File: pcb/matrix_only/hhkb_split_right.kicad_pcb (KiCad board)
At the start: 2 copper layers, 171.7 x 97.4 mm, 83 parts, among them SW1 CPG151101S11-2, SW10 CPG151101S11-2, SW11 CPG151101S11-2, SW12 CPG151101S11-2, SW13 CPG151101S11-2, SW14 CPG151101S11-2, SW15 CPG151101S11-2, SW16 CPG151101S11-2, SW17 CPG151101S11-2, SW18 CPG151101S11-2, SW19 CPG151101S11-2, SW2 CPG151101S11-2, SW20 CPG151101S11-2, SW21 CPG151101S11-2, SW22 CPG151101S11-2, SW23 CPG151101S11-2, SW24 CPG151101S11-2, SW25 CPG151101S11-2, SW26 CPG151101S11-2, SW27 CPG151101S11-2, SW28 CPG151101S11-2, SW29 CPG151101S11-2, SW3 CPG151101S11-2, SW30 CPG151101S11-2, SW31 CPG151101S11-2, SW32 CPG151101S11-2, SW33 CPG151101S11-2, SW34 CPG151101S11-2, SW4 CPG151101S11-2, SW5 CPG151101S11-2, SW6 CPG151101S11-2, SW7 CPG151101S11-2, SW8 CPG151101S11-2, SW9 CPG151101S11-2, U1 74LVC595, U2 74LVC595

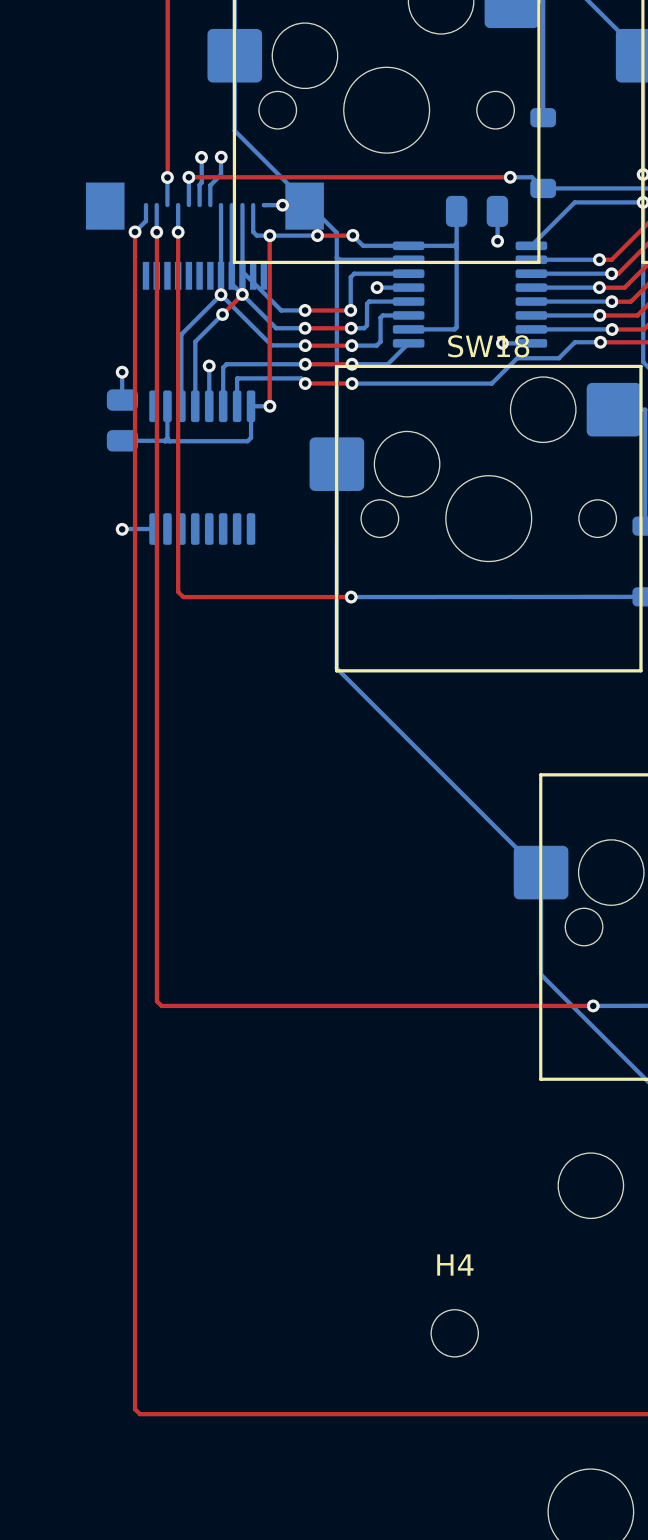
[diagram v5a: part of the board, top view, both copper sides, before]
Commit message: #19 右の J_DB 周りを利用者が引き直し、3 基板とも DRC 0 / 未配線 0
- COL0 の斜め線が回した J_DB の MP パッドを横切っていたのを MP の外（x=81 → y=82.3、SW10 の穴から 0.25mm 以上）へ逃がした
- φ0.5 の GND ビア 1 個を φ0.6 に
- 検査 457 緑・3 赤（右 J_DB とソケットの保守的占有範囲の重なり 1.63mm＝利用者の判断、露出ビアの打ち直し）。open-gaps #19 に記録
- 部品記録・DRC 記録・証拠ページを更新。gen_case.py の別セッションの変更は含めない

Co-Authored-By: Claude Fable 5 <noreply@anthropic.com>
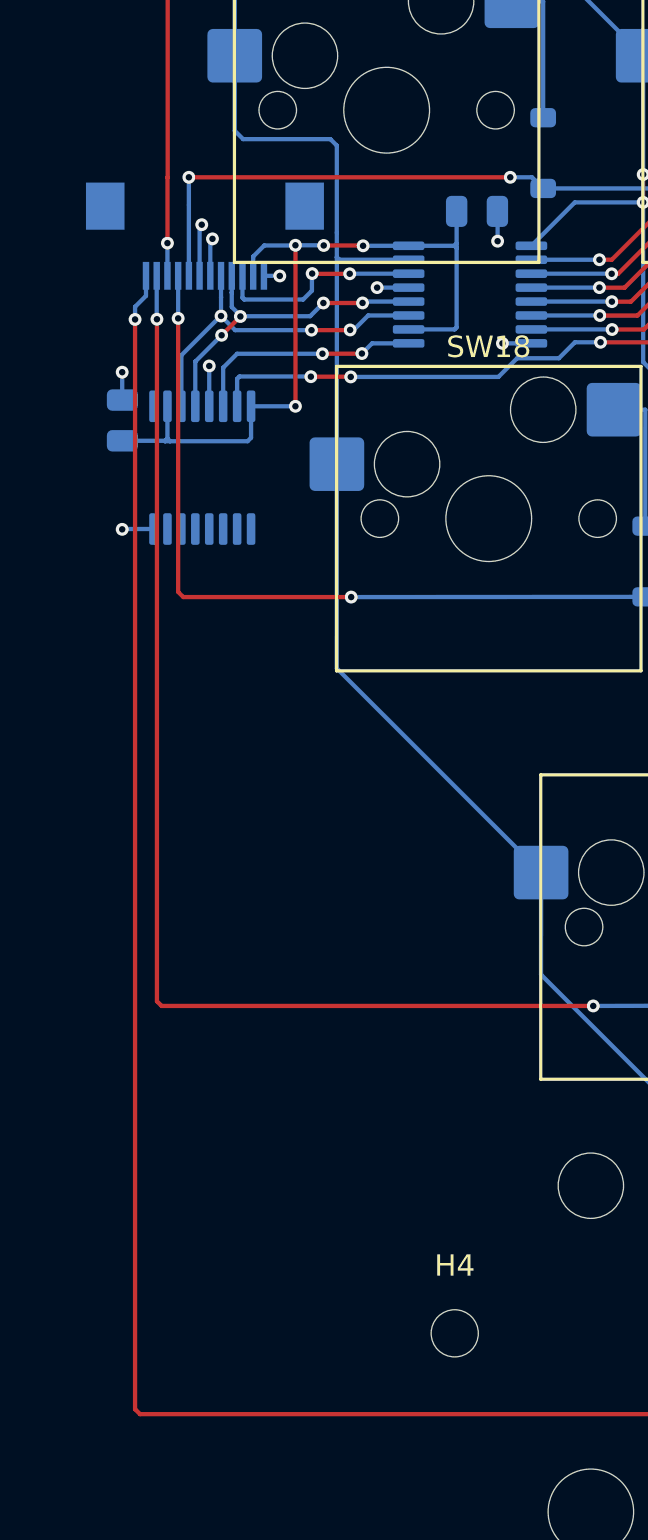
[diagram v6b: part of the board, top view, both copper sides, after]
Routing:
- net SPI_SCK: track 21.3 -> 16.2 mm
- net CS: track 20.0 -> 15.3 mm
- net SPI_MOSI: track 13.2 -> 9.78 mm
- net ROW_D: track 198.1 -> 194.8 mm
- net ROW_C: track 180.0 -> 183.3 mm
- net ROW_A: track 156.1 -> 159.4 mm
- net ROW_E: track 170.8 -> 167.5 mm
- net ROW_B: track 166.1 -> 162.8 mm
- net COL0: track 95.5 -> 97.9 mm
- net SPARE2: track 2.45 -> 1.77 mm

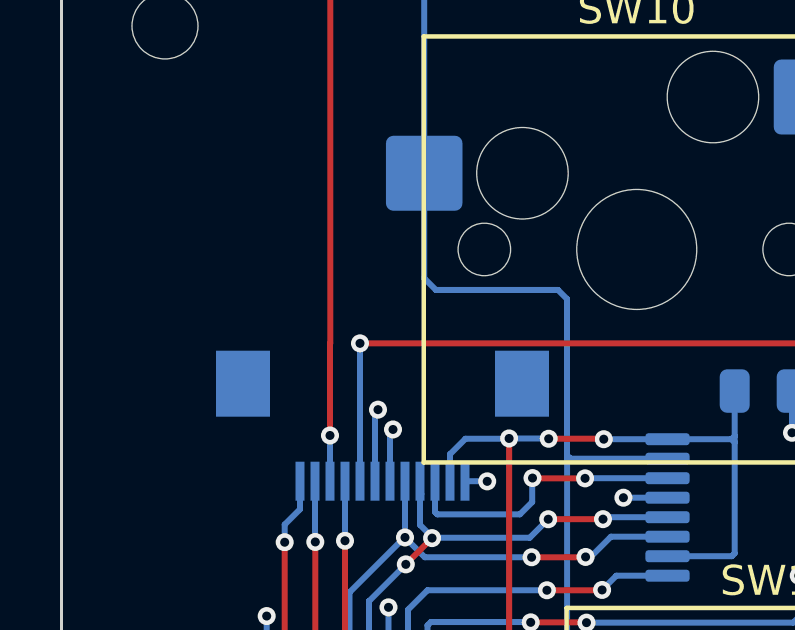
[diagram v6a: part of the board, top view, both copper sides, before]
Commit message: #49 利用者が左右の露出ビア（SPARE/SPARE2）を打ち直し。右の COL0 迂回と GND ビア径を当て直し、3 基板とも DRC 0
- 左右とも SPARE/SPARE2 が露出できるようになった（左 SCK は未だ）
- ⚠️ 打った場所はコネクタの奥側＝ケーブルの通り道。南側への移動を提案（open-gaps #19）

Co-Authored-By: Claude Fable 5 <noreply@anthropic.com>
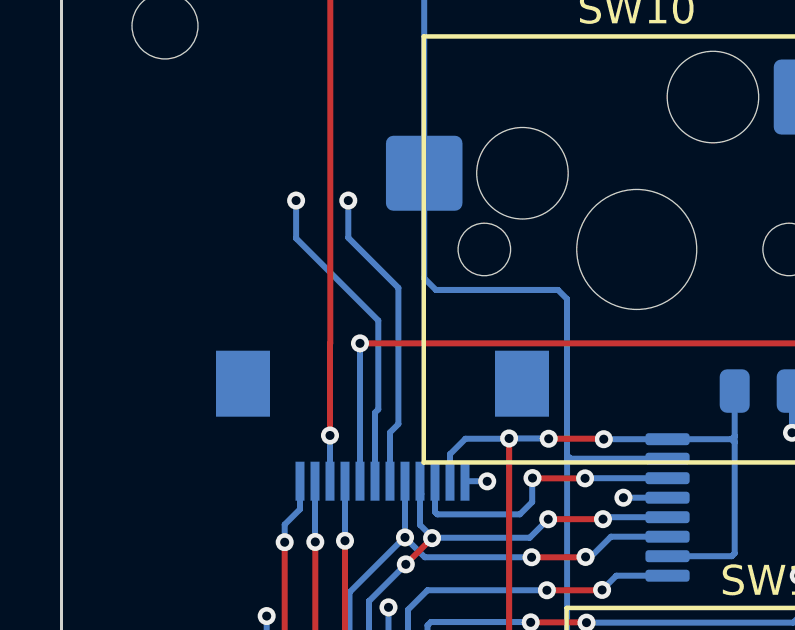
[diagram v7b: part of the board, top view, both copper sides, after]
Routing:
- net SPARE2: track 1.77 -> 10.2 mm
- net SPARE: track 2.43 -> 10.5 mm
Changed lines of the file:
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@@
+	)
+	(segment
+		(start 81 82.6)
+		(end 80.7 82.3)
+		(width 0.2)
+		(layer "B.Cu")
+		(net "COL0")
+	)
+	(segment
+		(start 81.0025 97.46)
+		(end 81.0025 88.0425)
+		(width 0.2)
+		(layer "B.Cu")
+		(net "COL0")
+	)
+	(segment
+		(start 81.0025 97.46)
+		(end 81 106.985)
+		(width 0.2)
+		(layer "B.Cu")
+		(net "COL0")
+	)
+	(segment
+		(start 81.12 87.925)
+		(end 81 87.81)
+		(width 0.2)
+		(layer "B.Cu")
+		(net "COL0")
+	)
+	(segment
+		(start 81 87.81)
+		(end 81 86.67)
+		(width 0.2)
+		(layer "B.Cu")
+		(net "COL0")
 	)
 	(segment
@@
 	)
 	(segment
-		(start 81.0025 97.46)
-		(end 81.0025 88.0425)
-		(width 0.2)
-		(layer "B.Cu")
-		(net "COL0")
-	)
-	(segment
-		(start 81.0025 97.46)
-		(end 81 106.985)
-		(width 0.2)
-		(layer "B.Cu")
-		(net "COL0")
-	)
-	(segment
-		(start 81.12 87.925)
-		(end 81 87.81)
+		(start 66.715 62.86)
+		(end 66.715 59.36)
 		(width 0.2)
 		(layer "B.Cu")
@@
 	)
 	(segment
+		(start 76.24 72.385)
+		(end 66.715 62.86)
+		(width 0.2)
+		(layer "B.Cu")
+		(net "COL0")
+	)
+	(segment
+		(start 84.35 87.925)
+		(end 81.12 87.925)
+		(width 0.2)
+		(layer "B.Cu")
+		(net "COL0")
+	)
+	(segment
+		(start 90.525 121.27)
+		(end 104.815 135.56)
+		(width 0.2)
+		(layer "B.Cu")
+		(net "COL0")
+	)
+	(segment
+		(start 81 88.04)
+		(end 81 87.81)
+		(width 0.2)
+		(layer "B.Cu")
+		(net "COL0")
+	)
+	(segment
+		(start 90.5275 116.51)
+		(end 90.525 121.27)
+		(width 0.2)
+		(layer "B.Cu")
+		(net "COL0")
+	)
+	(segment
+		(start 81 106.985)
+		(end 90.5275 116.51)
+		(width 0.2)
+		(layer "B.Cu")
+		(net "COL0")
+	)
+	(segment
+		(start 81.12 87.925)
+		(end 81 88.04)
+		(width 0.2)
+		(layer "B.Cu")
+		(net "COL0")
+	)
+	(segment
+		(start 76.24 81.91)
+		(end 76.24 72.385)
+		(width 0.2)
+		(layer "B.Cu")
+		(net "COL0")
+	)
+	(segment
 		(start 80.7 82.3)
 		(end 76.63 82.3)
@@
 	)
 	(segment
-		(start 66.715 62.86)
-		(end 66.715 59.36)
-		(width 0.2)
-		(layer "B.Cu")
-		(net "COL0")
-	)
-	(segment
-		(start 76.24 72.385)
-		(end 66.715 62.86)
-		(width 0.2)
-		(layer "B.Cu")
-		(net "COL0")
-	)
-	(segment
-		(start 84.35 87.925)
-		(end 81.12 87.925)
-		(width 0.2)
-		(layer "B.Cu")
-		(net "COL0")
-	)
-	(segment
-		(start 90.525 121.27)
-		(end 104.815 135.56)
-		(width 0.2)
-		(layer "B.Cu")
-		(net "COL0")
-	)
-	(segment
-		(start 81 82.6)
-		(end 80.7 82.3)
-		(width 0.2)
-		(layer "B.Cu")
-		(net "COL0")
-	)
-	(segment
-		(start 81 88.04)
-		(end 81 87.81)
-		(width 0.2)
-		(layer "B.Cu")
-		(net "COL0")
-	)
-	(segment
-		(start 81 87.81)
-		(end 81 86.67)
-		(width 0.2)
-		(layer "B.Cu")
-		(net "COL0")
-	)
-	(segment
-		(start 90.5275 116.51)
-		(end 90.525 121.27)
-		(width 0.2)
-		(layer "B.Cu")
-		(net "COL0")
-	)
-	(segment
-		(start 81 106.985)
-		(end 90.5275 116.51)
-		(width 0.2)
-		(layer "B.Cu")
-		(net "COL0")
-	)
-	(segment
-		(start 81.12 87.925)
-		(end 81 88.04)
-		(width 0.2)
-		(layer "B.Cu")
-		(net "COL0")
-	)
-	(segment
-		(start 76.24 81.91)
-		(end 76.24 72.385)
-		(width 0.2)
-		(layer "B.Cu")
-		(net "COL0")
-	)
-	(segment
 		(start 81.1 56.82)
 		(end 81.1 62.25)
@@
 	)
 	(via
-		(at 74.699999 86.29)
+		(at 71.97 79.32)
 		(size 0.6)
 		(drill 0.3)
@@
 	)
 	(segment
-		(start 74.699999 86.29)
-		(end 74.599999 86.39)
+		(start 71.97 80.58)
+		(end 74.71 83.32)
+		(width 0.2)
+		(layer "B.Cu")
+		(net "SPARE")
+	)
+	(segment
+		(start 71.97 79.32)
+		(end 71.97 80.58)
 		(width 0.2)
 		(layer "B.Cu")
@@
 		(net "SPARE")
 	)
-	(via
-		(at 75.199999 86.95)
-		(size 0.6)
-		(drill 0.3)
-		(layers "F.Cu" "B.Cu")
+	(segment
+		(start 74.71 86.279999)
+		(end 74.599999 86.39)
+		(width 0.2)
+		(layer "B.Cu")
+		(net "SPARE")
+	)
+	(segment
+		(start 74.71 83.32)
+		(end 74.71 86.279999)
+		(width 0.2)
+		(layer "B.Cu")
+		(net "SPARE")
+	)
+	(via
+		(at 73.71 79.32)
+		(size 0.6)
+		(drill 0.3)
+		(layers "F.Cu" "B.Cu")
+		(net "SPARE2")
+	)
+	(segment
+		(start 73.71 80.56)
+		(end 75.38 82.23)
+		(width 0.2)
+		(layer "B.Cu")
 		(net "SPARE2")
 	)
@@
 	)
 	(segment
-		(start 75.199999 86.95)
+		(start 75.38 82.23)
+		(end 75.38 86.769999)
+		(width 0.2)
+		(layer "B.Cu")
+		(net "SPARE2")
+	)
+	(segment
+		(start 75.38 86.769999)
 		(end 75.099999 87.05)
 		(width 0.2)
 		(layer "B.Cu")
+		(net "SPARE2")
+	)
+	(segment
+		(start 73.71 79.32)
+		(end 73.71 80.56)
+		(width 0.2)
+		(layer "B.Cu")

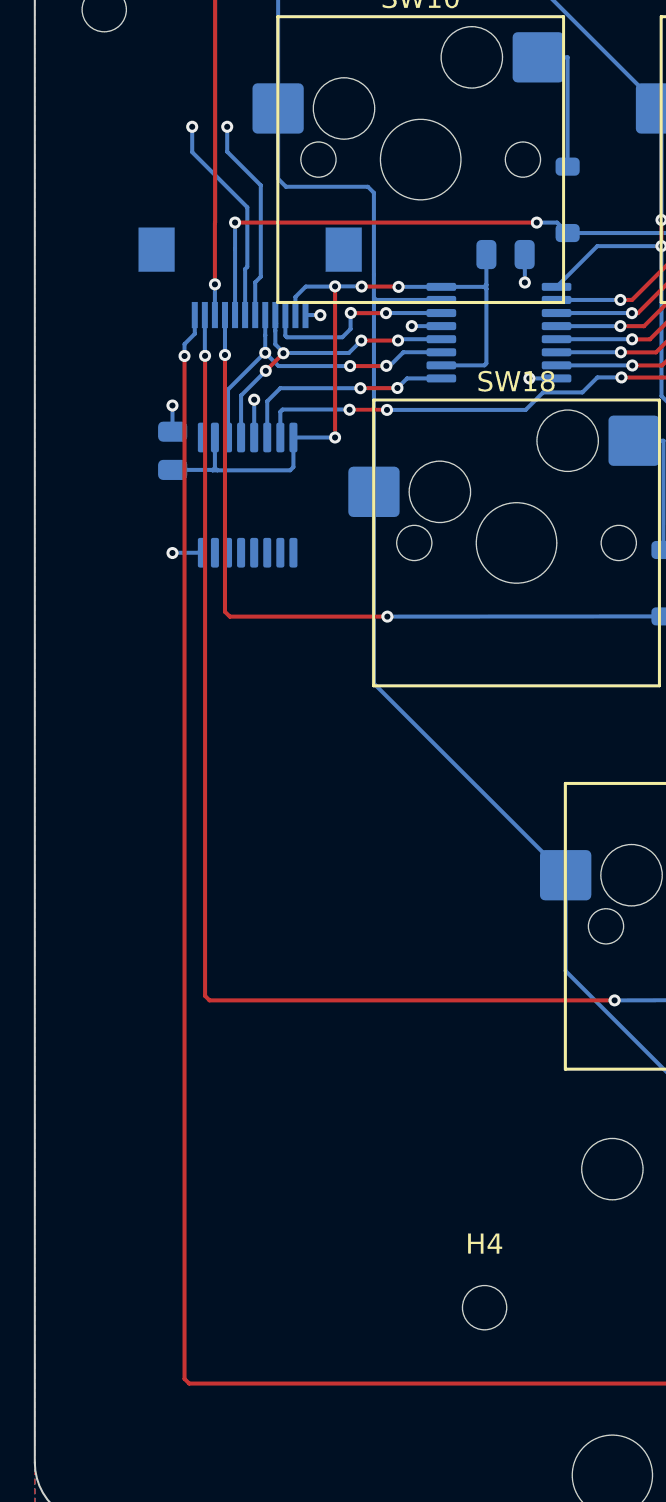
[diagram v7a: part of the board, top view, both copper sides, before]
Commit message: #19 決着: 右 J_DB を 1.63mm 手前へ（ソケットまで 3.9mm）、左右の配線と露出ビアを利用者が引き直し。3 基板とも DRC 0 / 未配線 0
- 右: MP パッドに当たった COL0 の迂回、V3V3 の裏面残骸 2 本を削除、MOSI ビアを 0.15mm 移動、混んだ V3V3 ビアを φ0.56（アニュラー 0.13）
- gen_pcb: 右 J_DB の dy を +1.235（中心 y=88.46）に
- 検査 458 緑・赤 1（左 SPI_SCK の露出のみ・任意）
- 記録・部品記録・DRC 記録・証拠ページを更新

Co-Authored-By: Claude Fable 5 <noreply@anthropic.com>
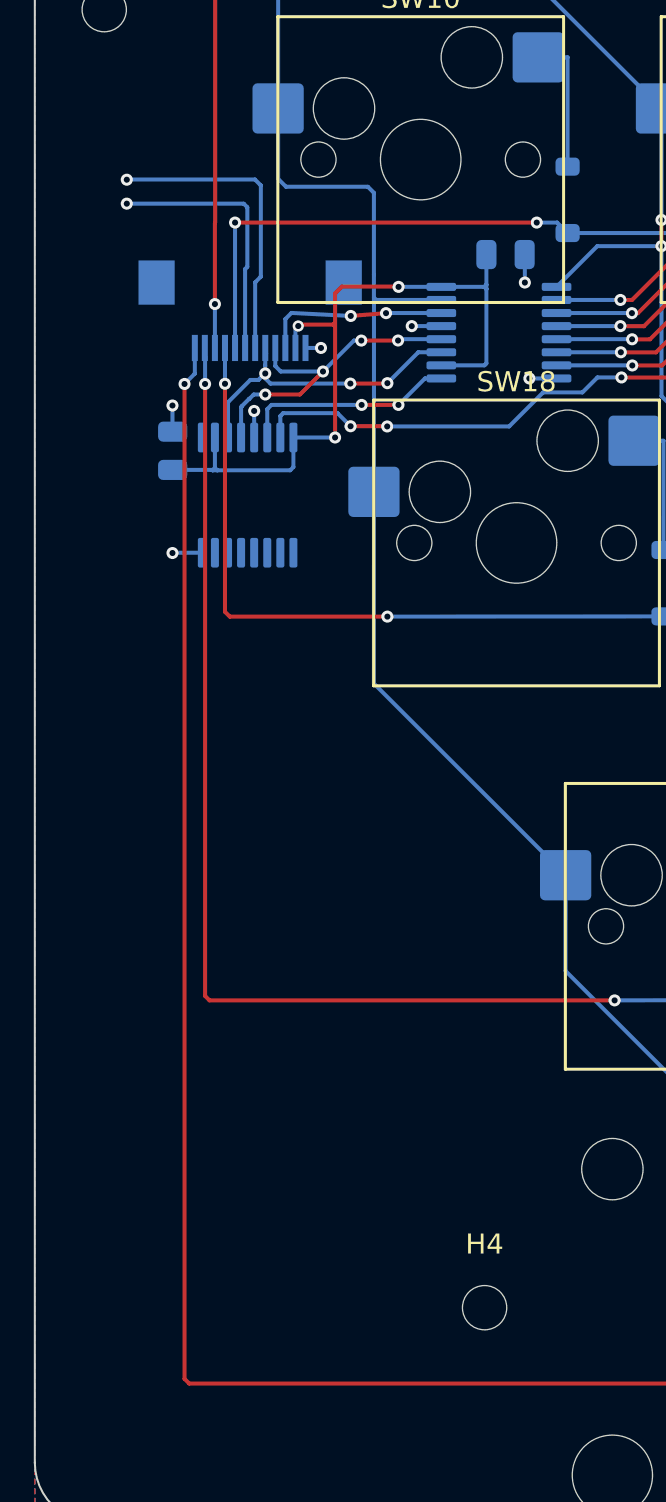
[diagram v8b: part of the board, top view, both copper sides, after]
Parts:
- moved J_DB 1.64 mm to (74.8, 88.5)
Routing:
- net SPARE2: track 10.2 -> 15.0 mm
- net SPARE: track 10.5 -> 13.1 mm
- net ROW_D: track 194.8 -> 192.8 mm
- net ROW_B: track 162.8 -> 160.9 mm
- net ROW_C: track 183.3 -> 185.0 mm
- net ROW_E: track 167.5 -> 165.8 mm
- net ROW_A: track 159.4 -> 161.1 mm
- net CS: track 15.3 -> 16.3 mm
- net SPI_SCK: track 16.2 -> 15.3 mm
- net COL8: track 205.0 -> 205.6 mm
- net GND: track 9.59 -> 9.06 mm
- net V3V3: track 37.5 -> 37.4 mm, vias 4 -> 3
